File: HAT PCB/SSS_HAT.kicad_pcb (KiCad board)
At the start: 2 copper layers, 30.8 x 74.8 mm, 26 parts, among them J1 ESP32_Connector_0, J2 ESP32_Connector_1, J3 CAN, J4 CAN, J5 I2C, J6 ADC_0, J7 ADC_1, U1 TJA1051T, U2 MCP3422Axx-xMS, U3 ICM-42688-P

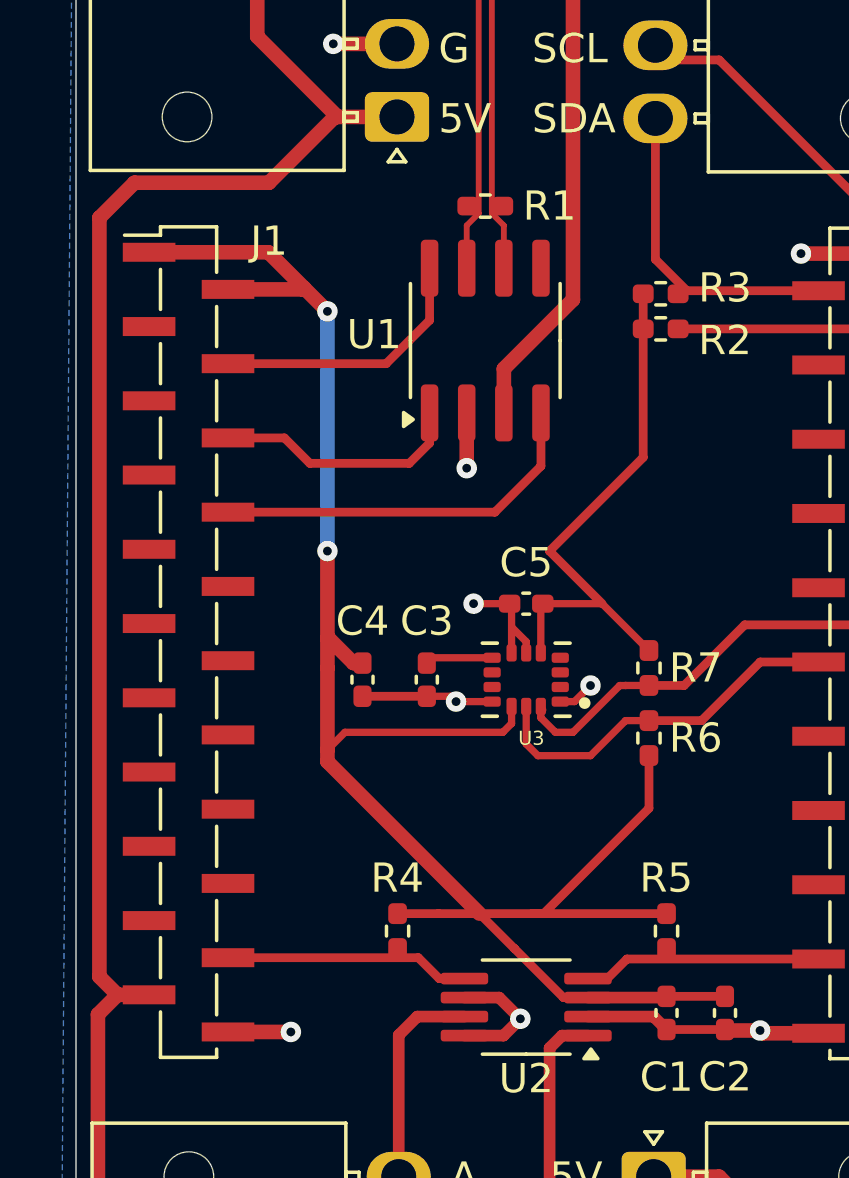
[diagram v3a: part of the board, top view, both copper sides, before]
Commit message: Changed a few traces and added measurements to PCB drawing
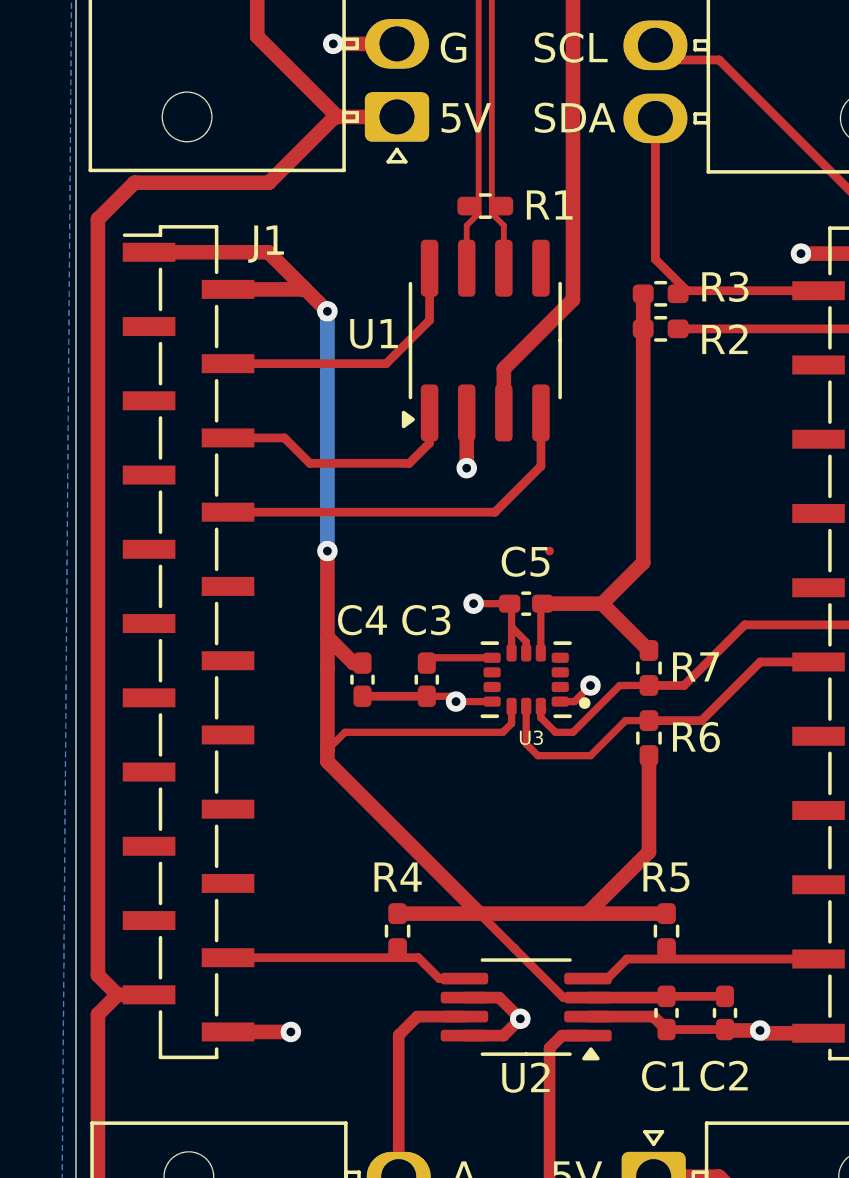
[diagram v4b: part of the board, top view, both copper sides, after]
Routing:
- net +3.3V: track 88.3 -> 85.7 mm

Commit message: A few minor layout changes
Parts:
- moved J7 1.92 mm to (136.8, 117.6)
- moved J6 1.90 mm to (146.8, 112.6)
- moved H3 1.80 mm to (153.2, 124.0)
- moved H4 1.80 mm to (130.4, 124.0)
- moved J3 0.60 mm to (138.1, 61.8)
- moved J5 0.54 mm to (146.8, 67.0)
- moved J4 0.54 mm to (136.8, 74.5)
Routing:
- net +5V: track 146.4 -> 148.2 mm
- net ADC_1: track 7.35 -> 9.15 mm
- net ADC_0: track 13.6 -> 15.4 mm
- net I2C_SDA: track 11.7 -> 10.7 mm
- net GND: track 42.3 -> 41.5 mm
- net I2C_SCL: track 25.9 -> 25.4 mm
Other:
- board size 30.8 x 74.8 mm -> 30.8 x 76.6 mm
- board text added: "3V3"
- board text added: "SSS HAT v1.0 Dallas Formula Racing"

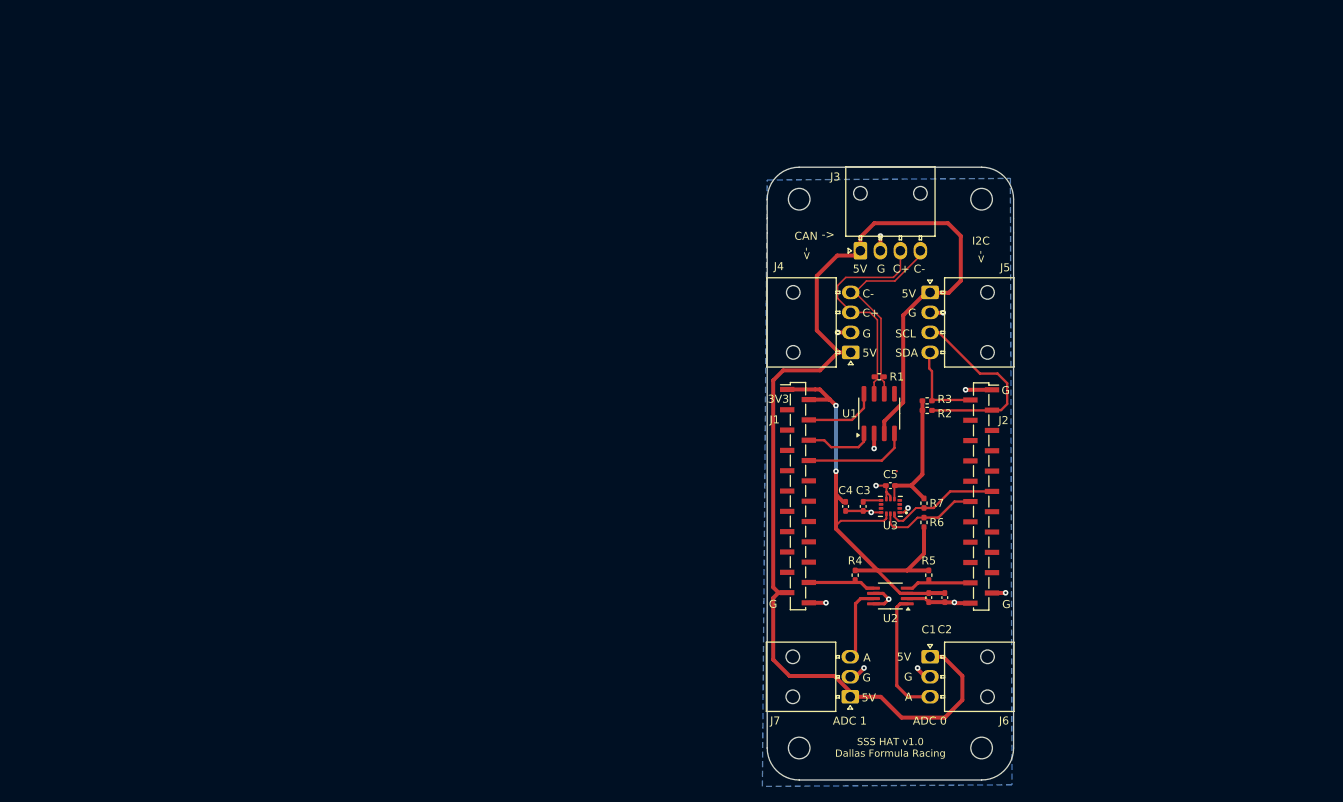
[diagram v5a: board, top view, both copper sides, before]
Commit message: Changed PCB drawing size & updated README.md images
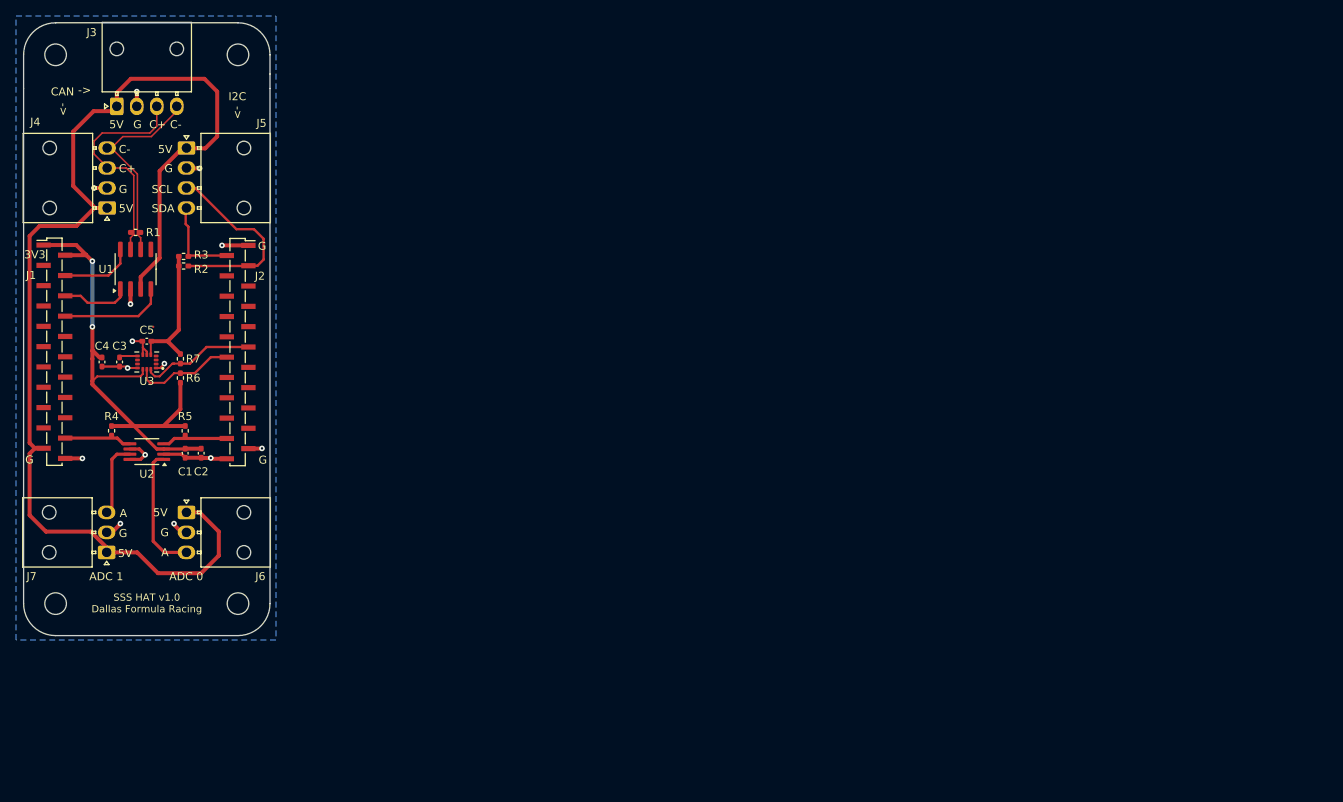
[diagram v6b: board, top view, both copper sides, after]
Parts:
- moved C5 94.7 mm to (48.9, 73.2)
- moved J3 94.7 mm to (45.1, 43.8)
- moved U2 94.7 mm to (48.9, 87.0)
- moved U3 94.7 mm to (48.9, 75.8)
- moved C3 94.7 mm to (45.5, 75.8)
- moved H1 94.7 mm to (37.5, 37.4)
- moved H4 94.7 mm to (37.5, 106.0)
- moved J1 94.7 mm to (37.3, 74.5)
- moved J2 94.7 mm to (60.2, 74.5)
- moved J4 94.7 mm to (43.9, 56.5)
- moved J7 94.7 mm to (43.8, 99.5)
- moved R1 94.7 mm to (47.5, 59.5)
- moved R2 94.7 mm to (53.5, 63.8)
- moved R3 94.7 mm to (53.5, 62.5)
- moved R4 94.7 mm to (44.5, 84.3)
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
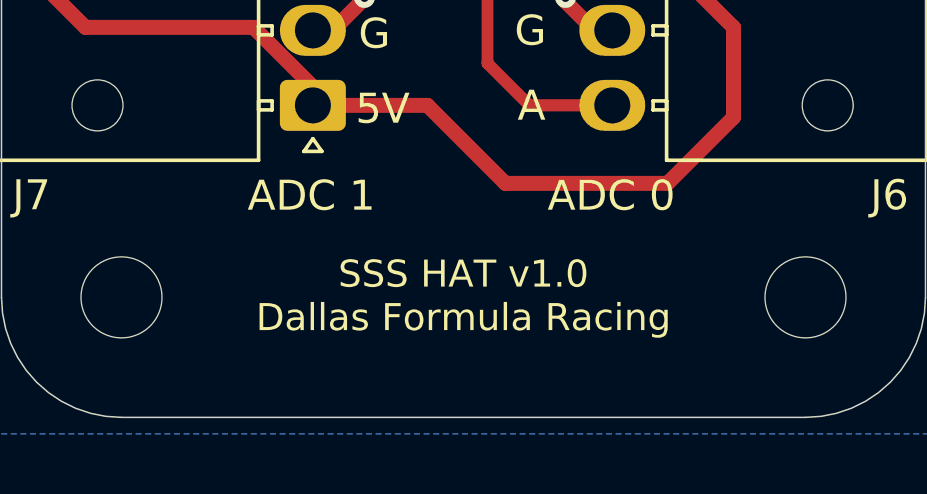
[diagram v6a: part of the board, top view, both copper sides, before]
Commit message: Added DFR logo and fixed GND connections
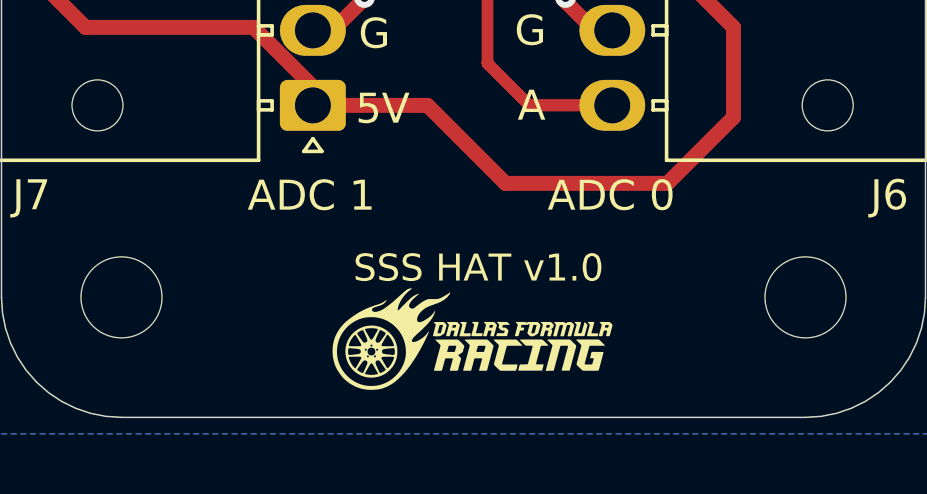
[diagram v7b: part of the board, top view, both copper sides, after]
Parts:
- added G***: LOGO, LOGO, F.Cu at (49.1, 107.5)
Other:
- board text added: "SSS HAT v1.0"
- board text removed: "SSS HAT v1.0 Dallas Formula Racing"

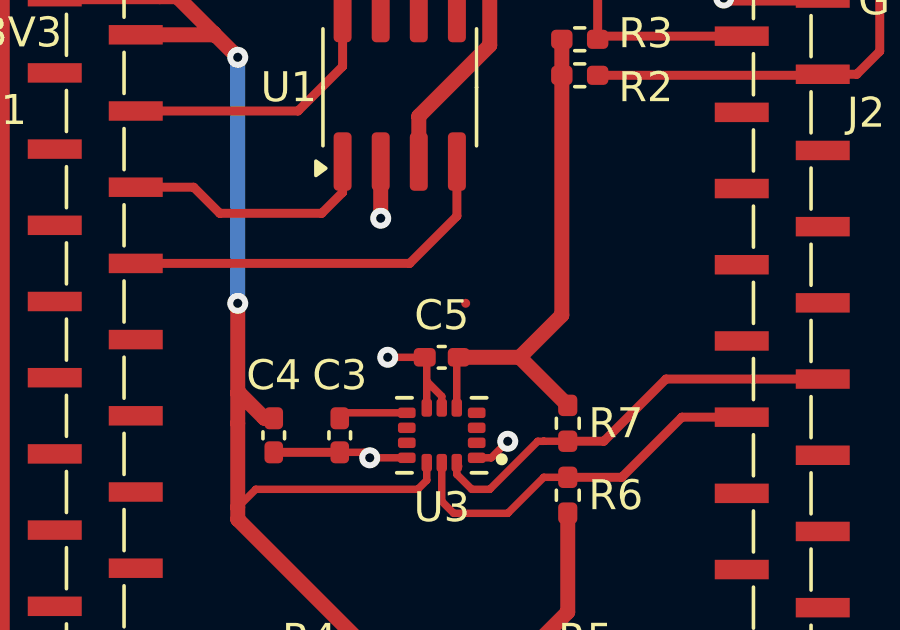
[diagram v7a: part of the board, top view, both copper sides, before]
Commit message: Added ADS8320EB/250 ADC
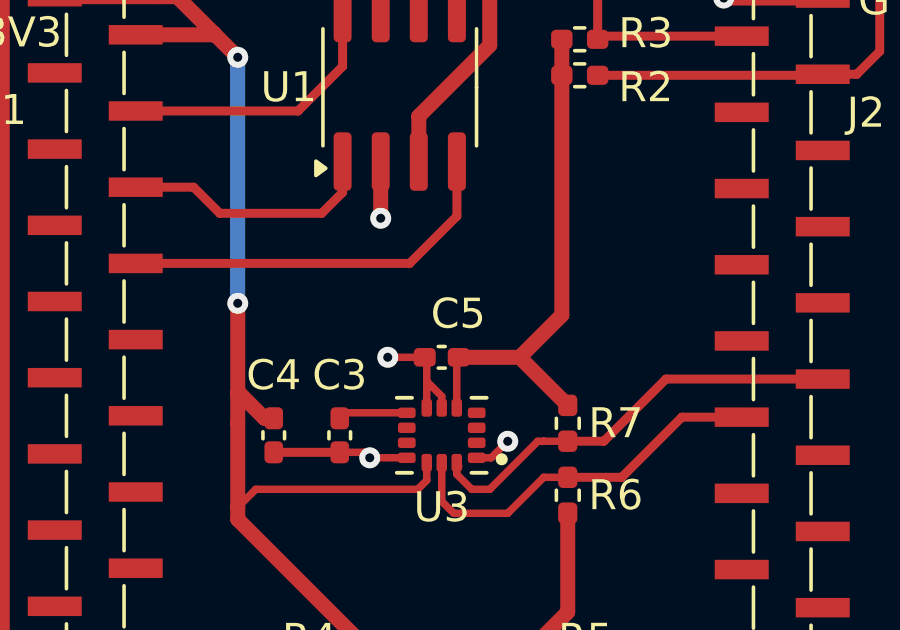
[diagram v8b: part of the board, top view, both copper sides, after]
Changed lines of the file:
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@@
 		(tags "capacitor handsolder")
 		(property "Reference" "C5"
-			(at 0 1.4 0)
+			(at -0.55 1.45 0)
 			(layer "F.SilkS")
 			(effects
@@
 		(layer "F.Cu")
 		(net 15)
-	)
-	(segment
-		(start 49.6475 71.35)
-		(end 49.65 71.35)
-		(width 0.3)
-		(layer "F.Cu")
-		(net 15)
